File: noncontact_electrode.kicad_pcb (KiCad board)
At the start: 4 copper layers, 26 x 26 mm, 10 parts, among them J1 CONN_01, J2 CONN_01, J3 CONN_01, J4 CONN_01, U1 LMP7702MM

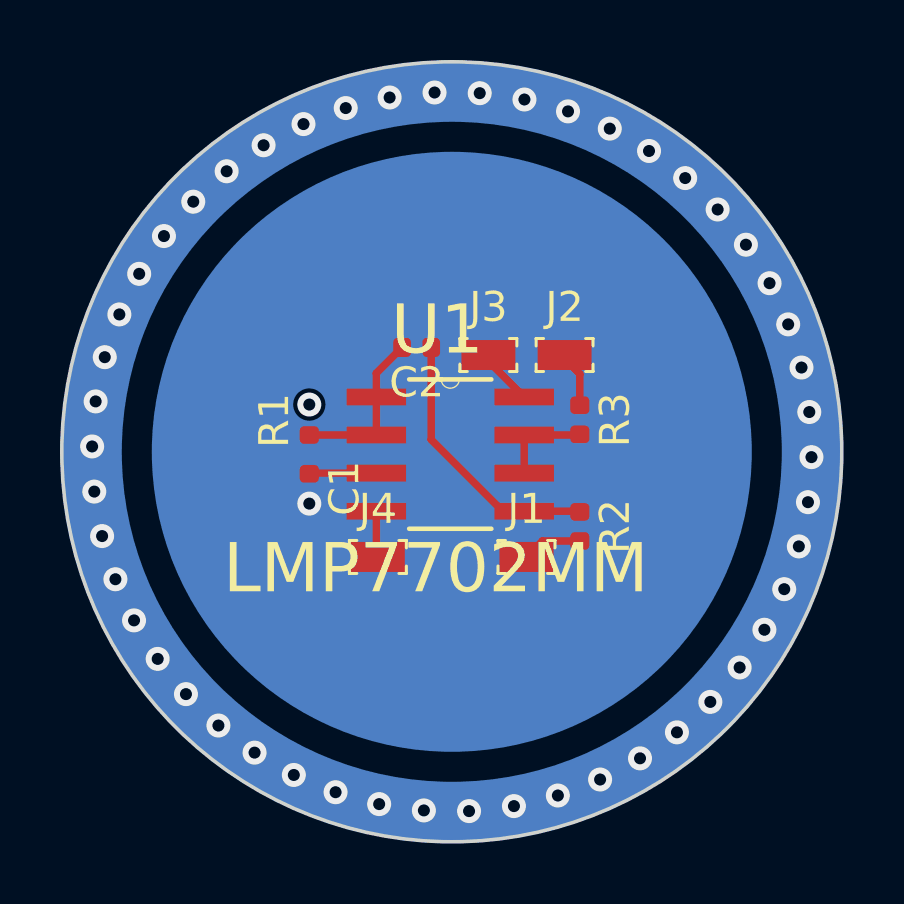
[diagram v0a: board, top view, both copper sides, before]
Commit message: B paste and mask added
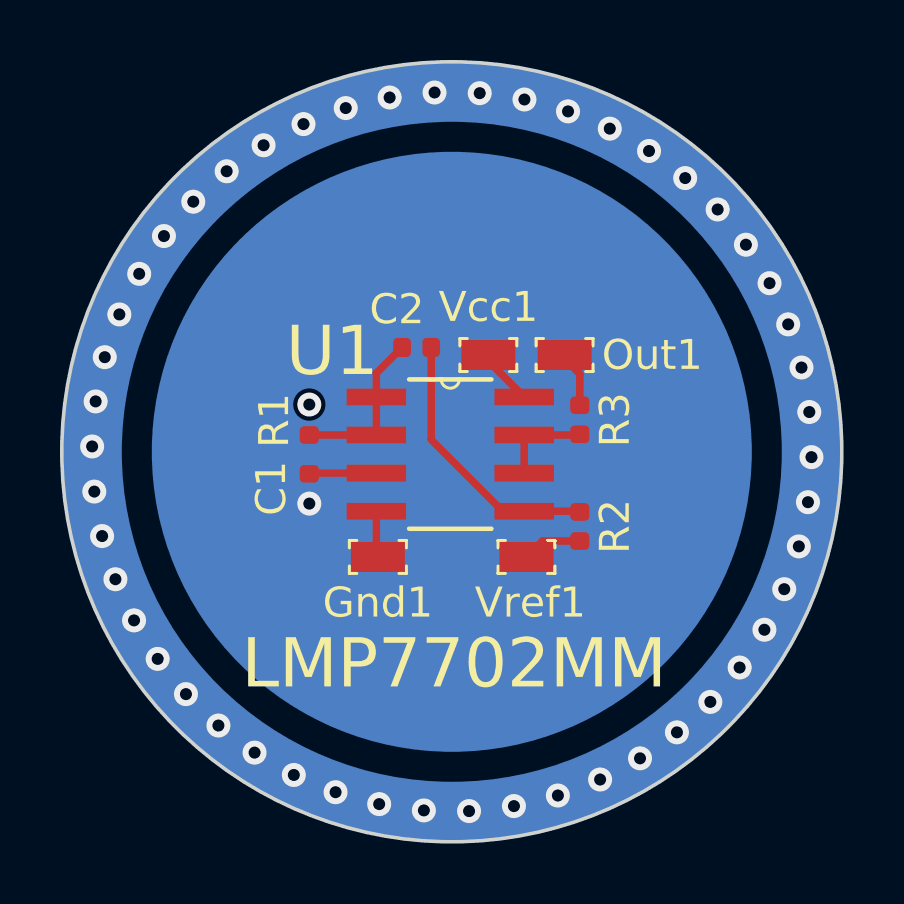
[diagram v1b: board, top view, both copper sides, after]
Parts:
- renumbered J4 to Gnd1, J2 to Out1, J3 to Vcc1, J1 to Vref1
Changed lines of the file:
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@@
     (2 In2.Cu signal)
     (31 B.Cu signal)
+    (32 B.Adhes user)
     (33 F.Adhes user)
+    (34 B.Paste user)
     (35 F.Paste user)
+    (36 B.SilkS user)
     (37 F.SilkS user)
+    (38 B.Mask user)
     (39 F.Mask user)
     (40 Dwgs.User user)
@@
     (46 B.CrtYd user)
     (47 F.CrtYd user)
+    (48 B.Fab user)
     (49 F.Fab user)
   )
@@
     (solder_mask_min_width 0.25)
     (aux_axis_origin 0 0)
-    (visible_elements FFFFFF7F)
+    (visible_elements 7FFFFFFF)
     (pcbplotparams
-      (layerselection 0x010a8_ffffffff)
+      (layerselection 0x010ec_ffffffff)
       (usegerberextensions true)
       (usegerberattributes false)
@@
   (net 2 "Net-(C2-Pad2)")
   (net 3 "Net-(C2-Pad1)")
-  (net 4 "Net-(J1-Pad1)")
-  (net 5 "Net-(J2-Pad1)")
-  (net 6 "Net-(R3-Pad2)")
-  (net 7 VDD)
-  (net 8 GND)
+  (net 4 "Net-(R3-Pad2)")
+  (net 5 VDD)
+  (net 6 GND)
+  (net 7 "Net-(Out1-Pad1)")
+  (net 8 "Net-(R2-Pad2)")
   (net_class Default "This is the default net class."
     (clearance 0.2)
@@
     (add_net GND)
     (add_net "Net-(C1-Pad1)")
-    (add_net "Net-(C1-Pad2)")
     (add_net "Net-(C2-Pad1)")
     (add_net "Net-(C2-Pad2)")
-    (add_net "Net-(J1-Pad1)")
-    (add_net "Net-(J2-Pad1)")
-    (add_net "Net-(R1-Pad2)")
+    (add_net "Net-(Out1-Pad1)")
+    (add_net "Net-(R2-Pad2)")
     (add_net "Net-(R3-Pad2)")
     (add_net VDD)
@@
     (at 97.536 103.505)
     (attr smd)
-    (fp_text reference J4 (at 0 -1.6) (layer F.SilkS)
+    (fp_text reference Gnd1 (at 0 1.524) (layer F.SilkS)
       (effects (font (size 1 1) (thickness 0.15)))
     )
@@
     )
     (pad 1 smd rect (at 0 0) (size 1.8 1) (layers F.Cu F.Paste F.Mask)
-      (net 8 GND))
+      (net 6 GND))
   )
   (module digikey-footprints:PROBE_PAD_0603 (layer F.Cu)
     (at 101.219 96.774)
     (attr smd)
-    (fp_text reference J3 (at 0 -1.6) (layer F.SilkS)
+    (fp_text reference Vcc1 (at 0 -1.6) (layer F.SilkS)
       (effects (font (size 1 1) (thickness 0.15)))
     )
@@
     )
     (pad 1 smd rect (at 0 0) (size 1.8 1) (layers F.Cu F.Paste F.Mask)
-      (net 7 VDD))
+      (net 5 VDD))
   )
   (module LMP7721MA:SOIC127P600X175-8N (layer F.Cu)
     (at 99.949 100.076)
     (attr smd)
-    (fp_text reference U1 (at -0.43203 -4.14246) (layer F.SilkS)
+    (fp_text reference U1 (at -3.937 -3.429) (layer F.SilkS)
       (effects (font (size 1.6409 1.6409) (thickness 0.05)))
     )
-    (fp_text value LMP7702MM (at -0.48305 3.81352) (layer F.SilkS)
+    (fp_text value LMP7702MM (at 0.127 6.985) (layer F.SilkS)
       (effects (font (size 1.64151 1.64151) (thickness 0.05)))
     )
-    (fp_arc (start 0 -2.5019) (end -0.3048 -2.4892) (angle -180) (layer F.SilkS) (width 0))
+    (fp_arc (start 0 -2.5019) (end -0.3048 -2.4892) (angle -180) (layer F.SilkS) (width 0.1))
     (fp_line (start -0.3048 -2.4892) (end -1.3716 -2.4892) (layer F.SilkS) (width 0.1524))
     (fp_line (start 1.3716 -2.4892) (end -0.3048 -2.4892) (layer F.SilkS) (width 0.1524))
     (fp_line (start -1.3716 2.4892) (end 1.3716 2.4892) (layer F.SilkS) (width 0.1524))
-    (fp_arc (start 0 -2.5019) (end -0.3048 -2.4892) (angle -180) (layer Eco2.User) (width 0))
+    (fp_arc (start 0 -2.5019) (end -0.3048 -2.4892) (angle -180) (layer Eco2.User) (width 0.1))
     (fp_line (start -1.9812 -2.4892) (end -1.9812 2.4892) (layer Eco2.User) (width 0.1524))
     (fp_line (start -0.3048 -2.4892) (end -1.9812 -2.4892) (layer Eco2.User) (width 0.1524))
@@
     (fp_line (start -1.9812 -1.651) (end -1.9812 -2.159) (layer Eco2.User) (width 0.1524))
     (pad 8 smd rect (at 2.4638 -1.905) (size 1.9812 0.5588) (layers F.Cu F.Paste F.Mask)
-      (net 7 VDD))
+      (net 5 VDD))
     (pad 7 smd rect (at 2.4638 -0.635) (size 1.9812 0.5588) (layers F.Cu F.Paste F.Mask)
-      (net 6 "Net-(R3-Pad2)"))
+      (net 4 "Net-(R3-Pad2)"))
     (pad 6 smd rect (at 2.4638 0.635) (size 1.9812 0.5588) (layers F.Cu F.Paste F.Mask)
-      (net 6 "Net-(R3-Pad2)"))
+      (net 4 "Net-(R3-Pad2)"))
     (pad 5 smd rect (at 2.4638 1.905) (size 1.9812 0.5588) (layers F.Cu F.Paste F.Mask)
       (net 3 "Net-(C2-Pad1)"))
     (pad 4 smd rect (at -2.4638 1.905) (size 1.9812 0.5588) (layers F.Cu F.Paste F.Mask)
-      (net 8 GND))
+      (net 6 GND))
     (pad 3 smd rect (at -2.4638 0.635) (size 1.9812 0.5588) (layers F.Cu F.Paste F.Mask)
       (net 1 "Net-(C1-Pad1)"))
@@
     (fp_line (start -0.5 0.25) (end -0.5 -0.25) (layer F.Fab) (width 0.1))
     (pad 2 smd roundrect (at 0.485 0 270) (size 0.59 0.64) (layers F.Cu F.Paste F.Mask) (roundrect_rratio 0.25)
-      (net 6 "Net-(R3-Pad2)"))
+      (net 4 "Net-(R3-Pad2)"))
     (pad 1 smd roundrect (at -0.485 0 270) (size 0.59 0.64) (layers F.Cu F.Paste F.Mask) (roundrect_rratio 0.25)
-      (net 5 "Net-(J2-Pad1)"))
+      (net 7 "Net-(Out1-Pad1)"))
     (model ${KISYS3DMOD}/Resistor_SMD.3dshapes/R_0402_1005Metric.wrl
       (at (xyz 0 0 0))
@@
     (fp_line (start -0.5 0.25) (end -0.5 -0.25) (layer F.Fab) (width 0.1))
     (pad 2 smd roundrect (at 0.485 0 270) (size 0.59 0.64) (layers F.Cu F.Paste F.Mask) (roundrect_rratio 0.25)
-      (net 4 "Net-(J1-Pad1)"))
+      (net 8 "Net-(R2-Pad2)"))
     (pad 1 smd roundrect (at -0.485 0 270) (size 0.59 0.64) (layers F.Cu F.Paste F.Mask) (roundrect_rratio 0.25)
       (net 3 "Net-(C2-Pad1)"))
@@
     (at 103.759 96.774)
     (attr smd)
-    (fp_text reference J2 (at 0 -1.6) (layer F.SilkS)
+    (fp_text reference Out1 (at 2.921 0) (layer F.SilkS)
       (effects (font (size 1 1) (thickness 0.15)))
     )
@@
     )
     (pad 1 smd rect (at 0 0) (size 1.8 1) (layers F.Cu F.Paste F.Mask)
-      (net 5 "Net-(J2-Pad1)"))
+      (net 7 "Net-(Out1-Pad1)"))
   )
   (module digikey-footprints:PROBE_PAD_0603 (layer F.Cu)
     (at 102.489 103.505)
     (attr smd)
-    (fp_text reference J1 (at 0 -1.6) (layer F.SilkS)
+    (fp_text reference Vref1 (at 0.127 1.524) (layer F.SilkS)
       (effects (font (size 1 1) (thickness 0.15)))
     )
@@
     )
     (pad 1 smd rect (at 0 0) (size 1.8 1) (layers F.Cu F.Paste F.Mask)
-      (net 4 "Net-(J1-Pad1)"))
+      (net 8 "Net-(R2-Pad2)"))
   )
   (module Capacitor_SMD:C_0402_1005Metric (layer F.Cu)
@@
     (tags capacitor)
     (attr smd)
-    (fp_text reference C2 (at 0 -1.17) (layer F.SilkS)
+    (fp_text reference C2 (at 0.658 1.27) (layer F.SilkS)
       (effects (font (size 1 1) (thickness 0.15)))
     )
@@
     (tags capacitor)
     (attr smd)
-    (fp_text reference C1 (at 0 -1.17 90) (layer F.SilkS)
+    (fp_text reference C1 (at 0 1.27 90) (layer F.SilkS)
       (effects (font (size 1 1) (thickness 0.15)))
     )
@@
   (segment (start 104.244 101.981) (end 104.267 102.004) (width 0.25) (layer F.Cu) (net 3))
   (segment (start 102.4128 101.981) (end 104.244 101.981) (width 0.25) (layer F.Cu) (net 3))
-  (segment (start 103.02 102.974) (end 102.489 103.505) (width 0.25) (layer F.Cu) (net 4))
-  (segment (start 104.267 102.974) (end 103.02 102.974) (width 0.25) (layer F.Cu) (net 4))
-  (segment (start 103.759 96.774) (end 103.759 96.901) (width 0.25) (layer F.Cu) (net 5))
-  (segment (start 103.759 96.901) (end 104.267 97.409) (width 0.25) (layer F.Cu) (net 5))
-  (segment (start 104.267 97.409) (end 104.267 98.448) (width 0.25) (layer F.Cu) (net 5))
-  (segment (start 104.244 99.441) (end 104.267 99.418) (width 0.25) (layer F.Cu) (net 6))
-  (segment (start 102.4128 99.441) (end 104.244 99.441) (width 0.25) (layer F.Cu) (net 6))
-  (segment (start 102.4128 100.711) (end 102.4128 99.441) (width 0.25) (layer F.Cu) (net 6))
-  (segment (start 101.219 96.9772) (end 102.4128 98.171) (width 0.25) (layer F.Cu) (net 7))
-  (segment (start 101.219 96.774) (end 101.219 96.9772) (width 0.25) (layer F.Cu) (net 7))
-  (segment (start 97.4852 103.4542) (end 97.536 103.505) (width 0.25) (layer F.Cu) (net 8))
-  (segment (start 97.4852 101.981) (end 97.4852 103.4542) (width 0.25) (layer F.Cu) (net 8))
+  (segment (start 103.02 102.974) (end 102.489 103.505) (width 0.25) (layer F.Cu) (net 8))
+  (segment (start 104.267 102.974) (end 103.02 102.974) (width 0.25) (layer F.Cu) (net 8))
+  (segment (start 103.759 96.774) (end 103.759 96.901) (width 0.25) (layer F.Cu) (net 7))
+  (segment (start 103.759 96.901) (end 104.267 97.409) (width 0.25) (layer F.Cu) (net 7))
+  (segment (start 104.267 97.409) (end 104.267 98.448) (width 0.25) (layer F.Cu) (net 7))
+  (segment (start 104.244 99.441) (end 104.267 99.418) (width 0.25) (layer F.Cu) (net 4))
+  (segment (start 102.4128 99.441) (end 104.244 99.441) (width 0.25) (layer F.Cu) (net 4))
+  (segment (start 102.4128 100.711) (end 102.4128 99.441) (width 0.25) (layer F.Cu) (net 4))
+  (segment (start 101.219 96.9772) (end 102.4128 98.171) (width 0.25) (layer F.Cu) (net 5))
+  (segment (start 101.219 96.774) (end 101.219 96.9772) (width 0.25) (layer F.Cu) (net 5))
+  (segment (start 97.4852 103.4542) (end 97.536 103.505) (width 0.25) (layer F.Cu) (net 6))
+  (segment (start 97.4852 101.981) (end 97.4852 103.4542) (width 0.25) (layer F.Cu) (net 6))
   (zone (net 0) (net_name "") (layer In1.Cu) (hatch edge 0.508)
     (connect_pads (clearance 0.508))
